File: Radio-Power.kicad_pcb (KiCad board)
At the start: 2 copper layers, 52.7 x 45.7 mm, 17 parts, among them J1 Input, J2 Radio Power, Q1 BS170, Q2 FQP27P06, Q3 BS170, U1 L7805, U2 ATtiny85-20PU

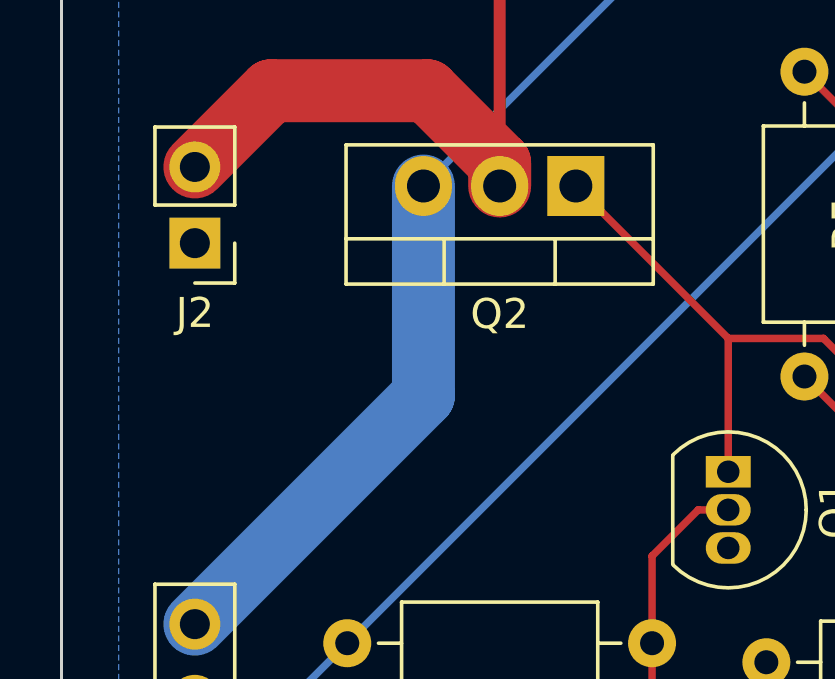
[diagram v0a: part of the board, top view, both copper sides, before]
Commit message: Forgot a resistor
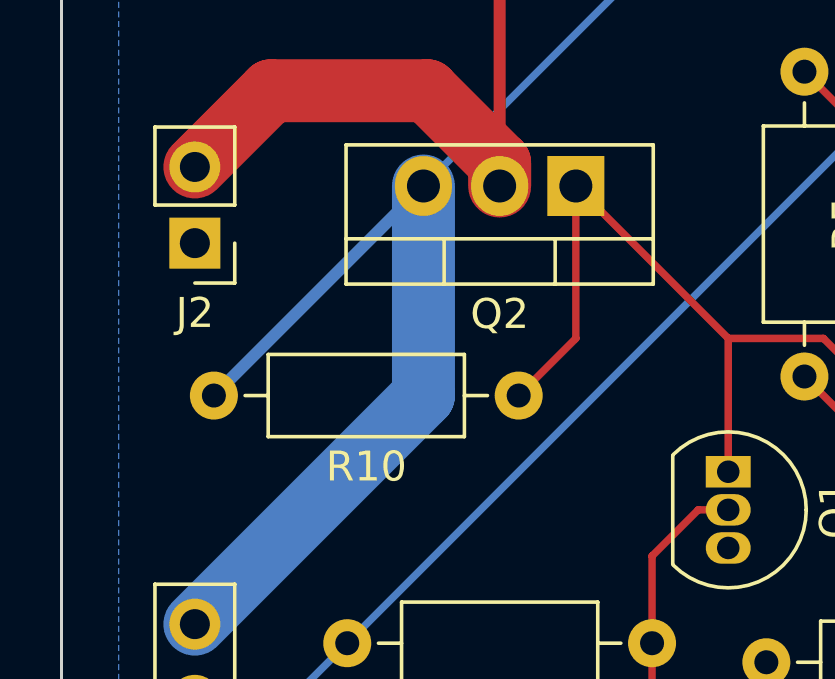
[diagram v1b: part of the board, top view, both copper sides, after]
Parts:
- added R10: 10K, Resistor_THT:R_Axial_DIN0207_L6.3mm_D2.5mm_P10.16mm_Horizontal, F.Cu at (29.8, 42.5)
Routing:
- net Bat+: track 41.8 -> 51.6 mm
- net Net-(Q1-Pad1): track 21.1 -> 28.9 mm
